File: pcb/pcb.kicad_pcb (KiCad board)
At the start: 2 copper layers, 299.5 x 123 mm, 72 parts

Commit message: A  RP2040_Minimal.kicad_sym A  RP2040_minimal.pretty/8-USON-Handsolder.kicad_mod A  RP2040_minimal.pretty/8-USON.kicad_mod A  RP2040_minimal.pretty/C_0402_1005Metric.kicad_mod A  RP2040_minimal.pretty/C_0603_1608Metric.kicad_mod A  RP2040_minimal.pretty/C_0603_1608Metric_Pad1.08x0.95mm_HandSolder.kicad_mod A  RP2040_minimal.pretty/C_1206_3216Metric.kicad_mod A  RP2040_minimal.pretty/Crystal_SMD_2520-4Pin_2.5x2.0mm-Handsolder.kicad_mod A  RP2040_minimal.pretty/Crystal_SMD_HC49-US.kicad_mod A  RP2040_minimal.pretty/D_0402_1005Metric.kicad_mod A  RP2040_minimal.pretty/D_SOD-523.kicad_mod A  RP2040_minimal.pretty/Diodes_U_DFN1212_3.kicad_mod A  RP2040_minimal.pretty/Diodes_U_DFN1212_3_Handsolder.kicad_mod A  RP2040_minimal.pretty/LED_0402_1005Metric.kicad_mod A  RP2040_minimal.pretty/LED_Driver_Mod_Conn.kicad_mod A  RP2040_minimal.pretty/LED_Driver_Mod_Conn_1.27.kicad_mod A  RP2040_minimal.pretty/Module_Conn_Regular.kicad_mod A  RP2040_minimal.pretty/Module_Conn_Regular2.kicad_mod A  RP2040_minimal.pretty/Module_Conn_Regular_Outline.kicad_mod A  RP2040_minimal.pretty/QFN-28-1EP_4x4mm_P0.4mm_EP2.3x2.3mm-Handsolder.kicad_mod A  RP2040_minimal.pretty/QFN-28-1EP_4x4mm_P0.4mm_EP2.3x2.3mm.kicad_mod A  RP2040_minimal.pretty/RP2040-QFN-56-Handsolder.kicad_mod A  RP2040_minimal.pretty/RP2040-QFN-56.kicad_mod A  RP2040_minimal.pretty/R_0402_1005Metric.kicad_mod A  RP2040_minimal.pretty/R_0603_1608Metric_Pad0.98x0.95mm_HandSolder.kicad_mod A  RP2040_minimal.pretty/SW_CK_KXT3.kicad_mod A  RP2040_minimal.pretty/SW_SPST_Panasonic_EVPAF.kicad_mod A  RP2040_minimal.pretty/SW_Side_EVPAV.kicad_mod A  RP2040_minimal.pretty/SW_XKB_TS_2030.kicad_mod A  RP2040_minimal.pretty/USB_Micro-B_Amphenol_10103594-0001LF_Horizontal_modified.kicad_mod A  RP2040_minimal.pretty/XSON-8-1EP_4x4mm.kicad_mod M  border.py M  notes/notes.md M  pcb/fp-lib-table M  pcb/pcb.kicad_pcb M  pcb/pcb.kicad_prl M  pcb/pcb.kicad_sch M  plate/plate.kicad_pcb M  plate/plate.kicad_sch R  tmr-footprints/Switch_Cutout2_MX.kic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
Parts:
- S64, S66: footprint tmr-lib:sw_lowpro_combo_MDT -> tmr-lib:sw_lowpro_combo_2u_MDT
- moved S63 2.32 mm to (95.6, 86.0), turned to -20 degrees
- moved S62 1.22 mm to (73.6, 76.0), turned to 0 degrees
- moved S68 1.22 mm to (199.5, 76.0), turned to 0 degrees
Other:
- board size 299.5 x 123 mm -> 299.2 x 113.4 mm

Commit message: M  border.py A  notes/keyfrequency M  pcb/pcb.kicad_pcb M  pcb/pcb.kicad_prl M  pcb/pcb.kicad_sch M  place.py A  tmr-footprints/LED-6028.kicad_mod D  tmr-footprints/LED_1206_THT.kicad_mod M  tmr-footprints/sw_lowpro_combo_2u_MDT.kicad_mod A  tmr-footprints/sw_lowpro_combo_2u_MDT_L.kicad_mod A  tmr-footprints/sw_lowpro_combo_2u_MDT_R.kicad_mod M  tmr-footprints/sw_lowpro_combo_MDT.kicad_mod M  tmr-footprints/sw_lowpro_combo_MDT_led.kicad_mod
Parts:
- S64: footprint tmr-lib:sw_lowpro_combo_2u_MDT -> tmr-lib:sw_lowpro_combo_2u_MDT_L
- S66: footprint tmr-lib:sw_lowpro_combo_2u_MDT -> tmr-lib:sw_lowpro_combo_2u_MDT_R
- moved S62 5.32 mm to (77.6, 79.5), turned to -20 degrees
- moved S59 4.25 mm to (11.4, 76.0)
- moved S68 3.91 mm to (197.8, 79.5), turned to 20 degrees
- moved S60 3.75 mm to (34.6, 76.0)
- moved S61 3.75 mm to (56.0, 76.0)
- moved S69 0.50 mm to (219.0, 76.0)
- moved S70 0.50 mm to (240.4, 76.0)
- moved S71 0.50 mm to (261.8, 76.0)
- moved S72 0.50 mm to (280.8, 76.0)
- turned S64 to -20 degrees
- turned S66 to 20 degrees
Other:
- board size 299.2 x 113.4 mm -> 299 x 113.3 mm

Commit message: M  border.py M  notes/components.md A  notes/mcu M  pcb/pcb.kicad_pcb M  place.py M  plate/plate.kicad_pcb M  plate/plate.kicad_sch
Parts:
- moved S1 2.38 mm to (16.6, 0.00)
- moved S60 0.40 mm to (35.0, 76.0)
- moved S61 0.40 mm to (56.4, 76.0)
- moved S71 0.10 mm to (261.9, 76.0)
- moved S72 0.10 mm to (280.9, 76.0)
- moved S59 0.10 mm to (11.3, 76.0)
- moved S69 0.10 mm to (219.1, 76.0)
- moved S70 0.10 mm to (240.5, 76.0)
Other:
- outline, holes or cut-outs redrawn

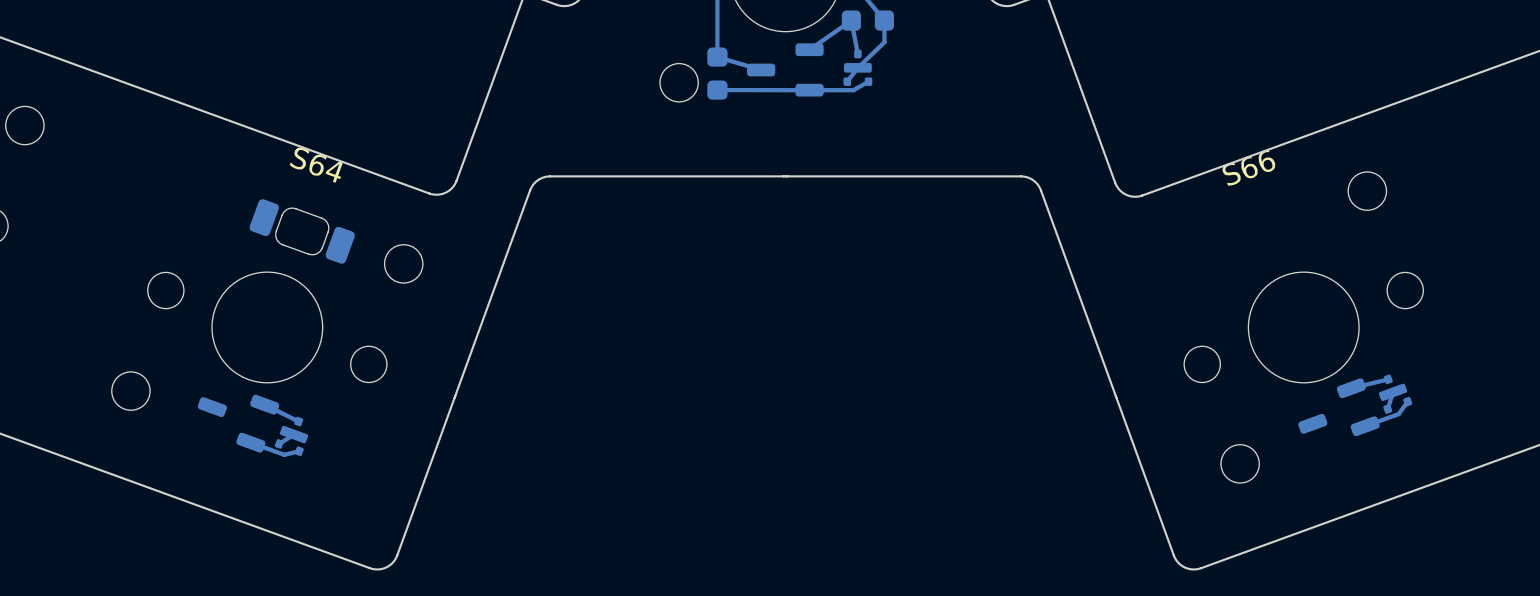
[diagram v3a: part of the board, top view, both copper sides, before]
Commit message: M  notes/components.md M  pcb/pcb.kicad_pcb M  pcb/pcb.kicad_sch M  place.py D  tmr-footprints/sw_lowpro_combo_2u_MDT.kicad_mod D  tmr-footprints/sw_lowpro_combo_2u_MDT_L.kicad_mod D  tmr-footprints/sw_lowpro_combo_2u_MDT_R.kicad_mod M  tmr-footprints/sw_lowpro_combo_MDT.kicad_mod A  tmr-footprints/sw_lowpro_stab_2u.kicad_mod M  tmr-symbols.kicad_sym
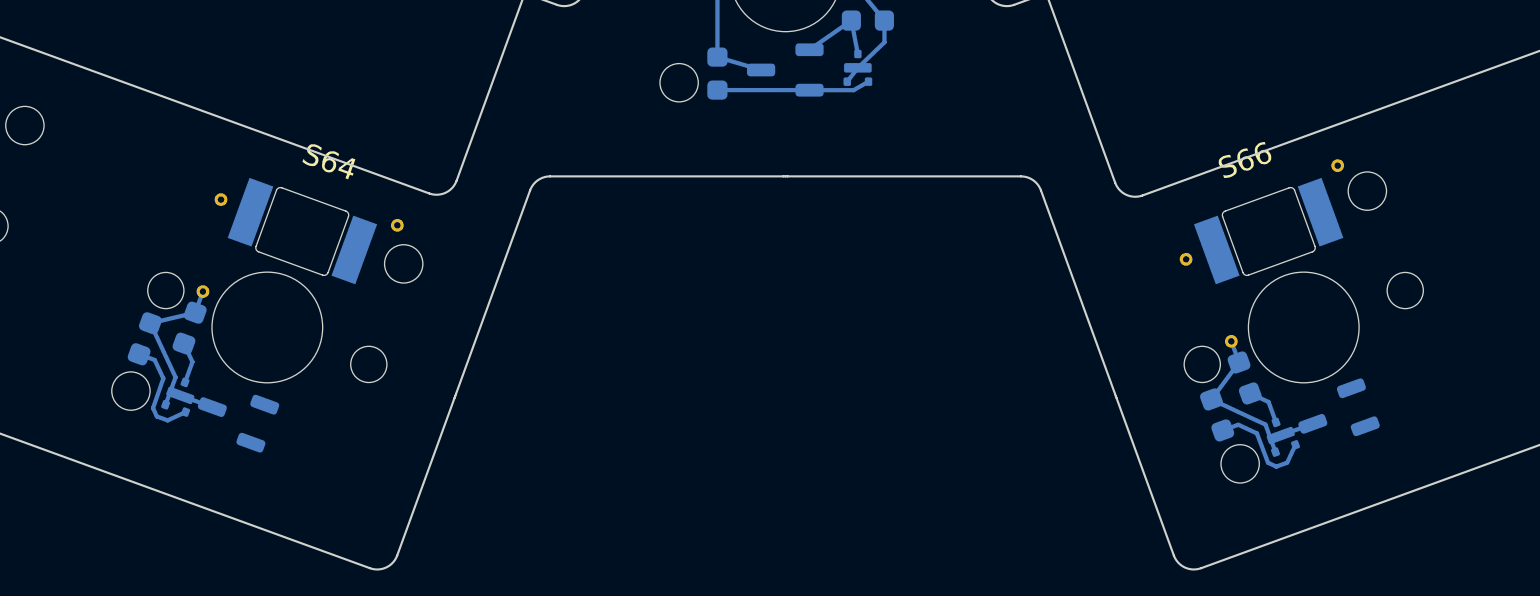
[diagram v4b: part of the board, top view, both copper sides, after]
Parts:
- added Stb1: TMR_switch_stab_2.0u, tmr-lib:sw_lowpro_stab_2u, F.Cu at (113.4, 92.5)
- added Stb2: TMR_switch_stab_2.0u, tmr-lib:sw_lowpro_stab_2u, F.Cu at (162.1, 92.5)
- S64: footprint tmr-lib:sw_lowpro_combo_2u_MDT_L -> tmr-lib:sw_lowpro_combo_MDT
- S66: footprint tmr-lib:sw_lowpro_combo_2u_MDT_R -> tmr-lib:sw_lowpro_combo_MDT

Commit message: M  border.py A  notes/cnc.md M  notes/components.md M  notes/nRF52840.md M  notes/notes.md A  notes/parts M  pcb/pcb.kicad_pcb M  plate/plate.kicad_pcb
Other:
- board size 299 x 113.3 mm -> 299.5 x 113.5 mm

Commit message: M  border.py M  notes/cnc.md M  notes/nRF52840.md M  notes/notes.md M  pcb/pcb.kicad_pcb M  pcb/pcb.kicad_sch M  pcb/sym-lib-table M  place.py M  plate/plate.kicad_pcb M  plate/plate.kicad_sch A  tmr-footprints/IS31FL3731-SSOP-28_5.3x10.2mm_P0.65mm.kicad_mod A  tmr-footprints/MCP3208-SOIC-16_3.9x9.9mm_P1.27mm.kicad_mod M  tmr-footprints/sw_lowpro_combo_MDT.kicad_mod D  tmr-footprints/sw_lowpro_combo_MDT_led.kicad_mod
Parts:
- added ADC1: MCP3208, tmr-lib:MCP3208-SOIC-16_3.9x9.9mm_P1.27mm, B.Cu at (56.1, 25.6)
- added ADC2: MCP3208, tmr-lib:MCP3208-SOIC-16_3.9x9.9mm_P1.27mm, F.Cu at (110.5, 129.5)
- added ADC3: MCP3208, tmr-lib:MCP3208-SOIC-16_3.9x9.9mm_P1.27mm, F.Cu at (119.0, 129.5)
- added ADC4: MCP3208, tmr-lib:MCP3208-SOIC-16_3.9x9.9mm_P1.27mm, F.Cu at (102.1, 141.2)
- added ADC5: MCP3208, tmr-lib:MCP3208-SOIC-16_3.9x9.9mm_P1.27mm, F.Cu at (110.5, 141.2)
- added ADC6: MCP3208, tmr-lib:MCP3208-SOIC-16_3.9x9.9mm_P1.27mm, F.Cu at (119.0, 141.2)
- added ADC7: MCP3208, tmr-lib:MCP3208-SOIC-16_3.9x9.9mm_P1.27mm, F.Cu at (102.1, 152.8)
- added ADC8: MCP3208, tmr-lib:MCP3208-SOIC-16_3.9x9.9mm_P1.27mm, F.Cu at (110.5, 152.8)
- added ADC9: MCP3208, tmr-lib:MCP3208-SOIC-16_3.9x9.9mm_P1.27mm, F.Cu at (119.0, 152.8)
- added D1: LED, tmr-lib:LED-6028, F.Cu at (55.3, 126.0)
- added D10: LED, tmr-lib:LED-6028, F.Cu at (55.3, 168.8)
- added D11: LED, tmr-lib:LED-6028, F.Cu at (55.3, 173.5)
- added D12: LED, tmr-lib:LED-6028, F.Cu at (55.3, 178.3)
- added D13: LED, tmr-lib:LED-6028, F.Cu at (63.1, 126.0)
- added D14: LED, tmr-lib:LED-6028, F.Cu at (63.1, 130.8)
- added D15: LED, tmr-lib:LED-6028, F.Cu at (63.1, 135.5)
- added D16: LED, tmr-lib:LED-6028, F.Cu at (63.1, 140.3)
- added D17: LED, tmr-lib:LED-6028, F.Cu at (63.1, 145.0)
- added D18: LED, tmr-lib:LED-6028, F.Cu at (63.1, 149.8)
- added D19: LED, tmr-lib:LED-6028, F.Cu at (63.1, 154.5)
- added D2: LED, tmr-lib:LED-6028, F.Cu at (55.3, 130.8)
- added D20: LED, tmr-lib:LED-6028, F.Cu at (63.1, 159.3)
- added D21: LED, tmr-lib:LED-6028, F.Cu at (63.1, 164.0)
- added D22: LED, tmr-lib:LED-6028, F.Cu at (63.1, 168.8)
- added D23: LED, tmr-lib:LED-6028, F.Cu at (63.1, 173.5)
- added D24: LED, tmr-lib:LED-6028, F.Cu at (63.1, 178.3)
- added D25: LED, tmr-lib:LED-6028, F.Cu at (70.8, 126.0)
- added D26: LED, tmr-lib:LED-6028, F.Cu at (70.8, 130.8)
- added D27: LED, tmr-lib:LED-6028, F.Cu at (70.8, 135.5)
- added D28: LED, tmr-lib:LED-6028, F.Cu at (70.8, 140.3)
- added D29: LED, tmr-lib:LED-6028, F.Cu at (70.8, 145.0)
- added D3: LED, tmr-lib:LED-6028, F.Cu at (55.3, 135.5)
- added D30: LED, tmr-lib:LED-6028, F.Cu at (70.8, 149.8)
- added D31: LED, tmr-lib:LED-6028, F.Cu at (70.8, 154.5)
- added D32: LED, tmr-lib:LED-6028, F.Cu at (70.8, 159.3)
- added D33: LED, tmr-lib:LED-6028, F.Cu at (70.8, 164.0)
- added D34: LED, tmr-lib:LED-6028, F.Cu at (70.8, 168.8)
- added D35: LED, tmr-lib:LED-6028, F.Cu at (70.8, 173.5)
- added D36: LED, tmr-lib:LED-6028, F.Cu at (70.8, 178.3)
- added D37: LED, tmr-lib:LED-6028, F.Cu at (78.6, 126.0)
- added D38: LED, tmr-lib:LED-6028, F.Cu at (78.6, 130.8)
- added D39: LED, tmr-lib:LED-6028, F.Cu at (78.6, 135.5)
- added D4: LED, tmr-lib:LED-6028, F.Cu at (55.3, 140.3)
- added D40: LED, tmr-lib:LED-6028, F.Cu at (78.6, 140.3)
- added D41: LED, tmr-lib:LED-6028, F.Cu at (78.6, 145.0)
- added D42: LED, tmr-lib:LED-6028, F.Cu at (78.6, 149.8)
- added D43: LED, tmr-lib:LED-6028, F.Cu at (78.6, 154.5)
- added D44: LED, tmr-lib:LED-6028, F.Cu at (78.6, 159.3)
- added D45: LED, tmr-lib:LED-6028, F.Cu at (78.6, 164.0)
- added D46: LED, tmr-lib:LED-6028, F.Cu at (78.6, 168.8)
- added D47: LED, tmr-lib:LED-6028, F.Cu at (78.6, 173.5)
- added D48: LED, tmr-lib:LED-6028, F.Cu at (78.6, 178.3)
- added D49: LED, tmr-lib:LED-6028, F.Cu at (86.4, 126.0)
- added D5: LED, tmr-lib:LED-6028, F.Cu at (55.3, 145.0)
- added D50: LED, tmr-lib:LED-6028, F.Cu at (86.4, 130.8)
- added D51: LED, tmr-lib:LED-6028, F.Cu at (86.4, 135.5)
- added D52: LED, tmr-lib:LED-6028, F.Cu at (86.4, 140.3)
- added D53: LED, tmr-lib:LED-6028, F.Cu at (86.4, 145.0)
- added D54: LED, tmr-lib:LED-6028, F.Cu at (86.4, 149.8)
- added D55: LED, tmr-lib:LED-6028, F.Cu at (86.4, 154.5)
- added D56: LED, tmr-lib:LED-6028, F.Cu at (86.4, 159.3)
- added D57: LED, tmr-lib:LED-6028, F.Cu at (86.4, 164.0)
- added D58: LED, tmr-lib:LED-6028, F.Cu at (86.4, 168.8)
- added D59: LED, tmr-lib:LED-6028, F.Cu at (86.4, 173.5)
- added D6: LED, tmr-lib:LED-6028, F.Cu at (55.3, 149.8)
- added D60: LED, tmr-lib:LED-6028, F.Cu at (86.4, 178.3)
- added D61: LED, tmr-lib:LED-6028, F.Cu at (94.1, 126.0)
- added D62: LED, tmr-lib:LED-6028, F.Cu at (94.1, 130.8)
- added D63: LED, tmr-lib:LED-6028, F.Cu at (94.1, 135.5)
- added D64: LED, tmr-lib:LED-6028, F.Cu at (94.1, 140.3)
- added D65: LED, tmr-lib:LED-6028, F.Cu at (94.1, 145.0)
- added D66: LED, tmr-lib:LED-6028, F.Cu at (94.1, 149.8)
- added D67: LED, tmr-lib:LED-6028, F.Cu at (94.1, 154.5)
- added D68: LED, tmr-lib:LED-6028, F.Cu at (94.1, 159.3)
- added D69: LED, tmr-lib:LED-6028, F.Cu at (94.1, 164.0)
- added D7: LED, tmr-lib:LED-6028, F.Cu at (55.3, 154.5)
- added D70: LED, tmr-lib:LED-6028, F.Cu at (94.1, 168.8)
- added D71: LED, tmr-lib:LED-6028, F.Cu at (94.1, 173.5)
- added D72: LED, tmr-lib:LED-6028, F.Cu at (94.1, 178.3)
- added D8: LED, tmr-lib:LED-6028, F.Cu at (55.3, 159.3)
- added D9: LED, tmr-lib:LED-6028, F.Cu at (55.3, 164.0)
- added LedDr1: IS31FL3731-QF, tmr-lib:IS31FL3731-SSOP-28_5.3x10.2mm_P0.65mm, F.Cu at (103.1, 164.4)
- added USBCon1: USB_TYPE_C_Receptacle_16P, Connector_USB:USB_C_Receptacle_XKB_U262-16XN-4BVC11, B.Cu at (28.5, -6.08)
- moved S1 2.38 mm to (19.0, 0.00)
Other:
- outline, holes or cut-outs redrawn

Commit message: M  border.py M  notes/notes.md M  pcb/pcb.kicad_pcb M  pcb/pcb.kicad_prl M  pcb/pcb.kicad_pro M  pcb/pcb.kicad_sch M  pcb/sym-lib-table M  place.py M  tmr-footprints/C_0603_1608Metric.kicad_mod D  tmr-footprints/C_0805_2012Metric.kicad_mod A  tmr-footprints/C_1206_3216Metric.kicad_mod A  tmr-footprints/IS31FL3731-RECESSED-SSOP-28_5.3x10.2mm_P0.65mm.kicad_mod M  tmr-footprints/JLC_Order_Num.kicad_mod M  tmr-footprints/LED-6028.kicad_mod A  tmr-footprints/MCP3208-RECESSED-SOIC-16_3.9x9.9mm_P1.27mm.kicad_mod M  tmr-footprints/MCP3208-SOIC-16_3.9x9.9mm_P1.27mm.kicad_mod A  tmr-footprints/MountingHole_5.3mm_M5_ISO14580_Pad_TopBottom.kicad_mod A  tmr-footprints/R_0603_1608Metric.kicad_mod A  tmr-footprints/SMTSO_M1.6.kicad_mod A  tmr-footprints/SW_B3U-3000P.kicad_mod A  tmr-footprints/sw_lowpro_gateron_MDT.kicad_mod M  tmr-symbols.kicad_sym
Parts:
- removed the ADC5 at (110.5, 141.2)
- added ADC3: MCP3208, tmr-lib:MCP3208-SOIC-16_3.9x9.9mm_P1.27mm, B.Cu at (48.1, 54.3)
- added C1: C_Small_US, tmr-lib:C_0603_1608Metric, F.Cu at (215.0, 94.0)
- added C10: 100nF, tmr-lib:C_0603_1608Metric, F.Cu at (215.0, 116.6)
- added C11: 100nF, tmr-lib:C_0603_1608Metric, F.Cu at (219.0, 94.0)
- added C12: 100nF, tmr-lib:C_0603_1608Metric, F.Cu at (219.0, 96.5)
- added C13: 100nF, tmr-lib:C_0603_1608Metric, F.Cu at (219.0, 99.0)
- added C14: 100nF, tmr-lib:C_0603_1608Metric, F.Cu at (219.0, 101.5)
- added C15: 100nF, tmr-lib:C_0603_1608Metric, F.Cu at (219.0, 104.0)
- added C16: 100nF, tmr-lib:C_0603_1608Metric, F.Cu at (219.0, 106.5)
- added C17: 100nF, tmr-lib:C_0603_1608Metric, F.Cu at (219.0, 109.1)
- added C18: 100nF, tmr-lib:C_0603_1608Metric, F.Cu at (219.0, 111.6)
- added C19: 2.2uF, tmr-lib:C_0603_1608Metric, F.Cu at (219.0, 114.1)
- added C2: C_Small_US, tmr-lib:C_0603_1608Metric, F.Cu at (215.0, 96.5)
- added C20: 1uF, tmr-lib:C_0603_1608Metric, F.Cu at (219.0, 116.6)
- added C21: 1uF, tmr-lib:C_0603_1608Metric, F.Cu at (223.1, 94.0)
- added C22: 100nF, tmr-lib:C_0603_1608Metric, F.Cu at (223.1, 96.5)
- added C23: 2.2uF, tmr-lib:C_0603_1608Metric, F.Cu at (223.1, 99.0)
- added C24: 10uF, tmr-lib:C_0603_1608Metric, F.Cu at (223.1, 101.5)
- added C25: 2.2uF, tmr-lib:C_0603_1608Metric, F.Cu at (223.1, 104.0)
- added C26: 1uF, tmr-lib:C_0603_1608Metric, F.Cu at (223.1, 106.5)
- added C27: 10uF, tmr-lib:C_1206_3216Metric, F.Cu at (206.5, 94.7)
- added C28: 10uF, tmr-lib:C_0603_1608Metric, F.Cu at (223.1, 109.1)
- added C29: 100nF, tmr-lib:C_0603_1608Metric, F.Cu at (223.1, 111.6)
- added C3: C_Small_US, tmr-lib:C_0603_1608Metric, F.Cu at (215.0, 99.0)
- added C30: 100nF, tmr-lib:C_0603_1608Metric, F.Cu at (223.1, 114.1)
- added C31: 15pF, tmr-lib:C_0603_1608Metric, F.Cu at (28.3, 62.9)
- added C32: 15pF, tmr-lib:C_0603_1608Metric, F.Cu at (28.6, 56.6)
- added C4: C_Small_US, tmr-lib:C_0603_1608Metric, F.Cu at (215.0, 101.5)
- added C5: C_Small_US, tmr-lib:C_0603_1608Metric, F.Cu at (215.0, 104.0)
- added C6: C_Small_US, tmr-lib:C_0603_1608Metric, F.Cu at (215.0, 106.5)
- added C7: C_Small_US, tmr-lib:C_0603_1608Metric, F.Cu at (215.0, 109.1)
- added C8: C_Small_US, tmr-lib:C_0603_1608Metric, F.Cu at (215.0, 111.6)
- added C9: C_Small_US, tmr-lib:C_0603_1608Metric, F.Cu at (215.0, 114.1)
- added H1: MountingHole, tmr-lib:MountingHole_5.3mm_M5_ISO14580_Pad_TopBottom, F.Cu at (85.5, 8.93)
- added H2: MountingHole, tmr-lib:MountingHole_5.3mm_M5_ISO14580_Pad_TopBottom, F.Cu at (237.5, 8.93)
- added H3: MountingHole, tmr-lib:MountingHole_5.3mm_M5_ISO14580_Pad_TopBottom, F.Cu at (291.6, 25.6)
- added H4: MountingHole, tmr-lib:MountingHole_5.3mm_M5_ISO14580_Pad_TopBottom, F.Cu at (12.3, 25.6)
- added H5: MountingHole, tmr-lib:MountingHole_5.3mm_M5_ISO14580_Pad_TopBottom, F.Cu at (99.8, 46.9)
- added H6: MountingHole, tmr-lib:MountingHole_5.3mm_M5_ISO14580_Pad_TopBottom, F.Cu at (175.8, 46.9)
- added H7: MountingHole, tmr-lib:MountingHole_5.3mm_M5_ISO14580_Pad_TopBottom, F.Cu at (1.90, 82.6)
- added H8: MountingHole, tmr-lib:MountingHole_5.3mm_M5_ISO14580_Pad_TopBottom, F.Cu at (251.2, 82.6)
- added Hs1: ~, tmr-lib:SMTSO_M1.6, F.Cu at (28.5, 8.93)
- added Hs10: ~, tmr-lib:SMTSO_M1.6, F.Cu at (275.5, 65.9)
- added Hs11, Hs12, Hs13, Hs14, Hs15, Hs16, Hs17, Hs18: ~, tmr-lib:SMTSO_M1.6, F.Cu at (0.00, 0.00)
- added Hs2: ~, tmr-lib:SMTSO_M1.6, F.Cu at (142.5, 8.93)
- added Hs3: ~, tmr-lib:SMTSO_M1.6, F.Cu at (275.5, 8.93)
- added Hs4: ~, tmr-lib:SMTSO_M1.6, F.Cu at (1.90, 76.0)
- added Hs5: ~, tmr-lib:SMTSO_M1.6, F.Cu at (61.8, 46.9)
- added Hs6: ~, tmr-lib:SMTSO_M1.6, F.Cu at (137.8, 46.9)
- added Hs7: ~, tmr-lib:SMTSO_M1.6, F.Cu at (86.4, 83.6)
- added Hs8: ~, tmr-lib:SMTSO_M1.6, F.Cu at (189.1, 83.6)
- added Hs9: ~, tmr-lib:SMTSO_M1.6, F.Cu at (209.0, 27.9)
- added JLC1: JLC_Order_Num, tmr-lib:JLC_Order_Num, F.Cu at (233.8, 161.6)
- added R1: 10k, tmr-lib:R_0603_1608Metric, B.Cu at (20.0, 91.5)
- added R10: 4.7k, tmr-lib:R_0603_1608Metric, B.Cu at (250.9, 68.6)
- added R11: 100k, tmr-lib:R_0603_1608Metric, B.Cu at (250.9, 71.1)
- added R12: 20k, tmr-lib:R_0603_1608Metric, B.Cu at (250.9, 73.6)
- added R13: 20k, tmr-lib:R_0603_1608Metric, B.Cu at (250.9, 76.1)
- added R14: 1k, tmr-lib:R_0603_1608Metric, B.Cu at (25.6, 61.6)
- added R2: 10k, tmr-lib:R_0603_1608Metric, B.Cu at (20.0, 94.0)
- added R3: 1k, tmr-lib:R_0603_1608Metric, B.Cu at (20.0, 96.5)
- added R4: 27R, tmr-lib:R_0603_1608Metric, B.Cu at (20.0, 99.1)
- added R5: 27R, tmr-lib:R_0603_1608Metric, B.Cu at (20.0, 101.6)
- added R6: 5.1k, tmr-lib:R_0603_1608Metric, B.Cu at (20.0, 104.1)
- added R7: 5.1k, tmr-lib:R_0603_1608Metric, B.Cu at (20.0, 106.6)
- added R8: 4.7k, tmr-lib:R_0603_1608Metric, B.Cu at (20.0, 109.1)
- added R9: 4.7k, tmr-lib:R_0603_1608Metric, B.Cu at (20.0, 111.6)
- added SW1: SW_DIP_x01_XKB_TS_2030, Button_Switch_SMD:SW_SPST_B3U-3000P, F.Cu at (1.95, 36.8)
- added SW2: SW_DIP_x01_XKB_TS_2030, Button_Switch_SMD:SW_SPST_B3U-3000P, F.Cu at (1.90, 41.9)
- added U1: RP2040, rp2040:RP2040-QFN-56, B.Cu at (21.4, 56.9)
- added U2: Memory_Flash_W25Q64_XSON, rp2040:8-USON, B.Cu at (20.5, 48.2)
- added U3: NCP114ASN330T1G, Package_SO:TSOP-5_1.65x3.05mm_P0.95mm, F.Cu at (1.99, 67.2)
- added X1: 12.000MHz, rp2040:Crystal_SMD_2520-4Pin_2.5x2.0mm-Handsolder, B.Cu at (28.7, 60.1)
- ADC2, ADC4, ADC6, ADC7, ADC8, ADC9: moved to B.Cu
- ADC5: renamed from ADC3; moved to B.Cu
- LedDr1: footprint tmr-lib:IS31FL3731-SSOP-28_5.3x10.2mm_P0.65mm -> rp2040:QFN-28-1EP_4x4mm_P0.4mm_EP2.3x2.3mm; moved to B.Cu
- S1, S10, S11, S12, S13, S14, S15, S16, S17, S18, S19, S2, S20, S21, S22, S23, S24, S25, S26, S27, S28, S29, S3, S30, S31, S32, S33, S34, S35, S36, S37, S38, S39, S4, S40, S41, S42, S43, S44, S45, S46, S47, S48, S49, S5, S50, S51, S52, S53, S54, S55, S56, S57, S58, S59, S6, S60, S61, S62, S63, S64, S65, S66, S67, S68, S69, S7, S70, S71, S72, S8, S9: footprint tmr-lib:sw_lowpro_combo_MDT -> tmr-lib:sw_lowpro_gateron_MDT
- moved D15 262.5 mm to (285.0, -4.75)
- moved D12 251.6 mm to (228.0, -4.75)
- moved D29 246.9 mm to (280.2, 14.2)
- moved D14 244.0 mm to (266.0, -4.75)
- moved D44 241.8 mm to (285.0, 33.2)
- moved D11 235.4 mm to (209.0, -4.75)
- moved D58 230.3 mm to (285.0, 52.2)
- moved D13 225.7 mm to (247.0, -4.75)
- moved D28 224.4 mm to (256.5, 14.2)
- moved D43 223.2 mm to (266.0, 33.2)
- moved D10 219.6 mm to (190.0, -4.75)
- moved D72 215.2 mm to (280.9, 71.2)
- moved D27 206.1 mm to (237.5, 14.2)
- moved D57 205.5 mm to (258.9, 52.2)
- moved D9 204.6 mm to (171.0, -4.75)
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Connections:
- ADC1 pad 14: unconnected-(ADC1-AGND-Pad14) -> GND
- ADC1 pad 15: unconnected-(ADC1-Vref-Pad15) -> +3V3
- ADC1 pad 16: unconnected-(ADC1-Vdd-Pad16) -> +3V3
- ADC1 pad 9: unconnected-(ADC1-DGND-Pad9) -> GND
- ADC2 pad 14: unconnected-(ADC2-AGND-Pad14) -> GND
- ADC2 pad 15: unconnected-(ADC2-Vref-Pad15) -> +3V3
- ADC2 pad 16: unconnected-(ADC2-Vdd-Pad16) -> +3V3
- ADC2 pad 9: unconnected-(ADC2-DGND-Pad9) -> GND
- ADC4 pad 14: unconnected-(ADC4-AGND-Pad14) -> GND
- ADC4 pad 15: unconnected-(ADC4-Vref-Pad15) -> +3V3
- ADC4 pad 16: unconnected-(ADC4-Vdd-Pad16) -> +3V3
- ADC4 pad 9: unconnected-(ADC4-DGND-Pad9) -> GND
- ADC5 pad 14: unconnected-(ADC3-AGND-Pad14) -> GND
- ADC5 pad 15: unconnected-(ADC3-Vref-Pad15) -> +3V3
- ADC5 pad 16: unconnected-(ADC3-Vdd-Pad16) -> +3V3
- ADC5 pad 9: unconnected-(ADC3-DGND-Pad9) -> GND
- ADC6 pad 14: unconnected-(ADC6-AGND-Pad14) -> GND
- ADC6 pad 15: unconnected-(ADC6-Vref-Pad15) -> +3V3
- ADC6 pad 16: unconnected-(ADC6-Vdd-Pad16) -> +3V3
- ADC6 pad 9: unconnected-(ADC6-DGND-Pad9) -> GND
- ADC7 pad 14: unconnected-(ADC7-AGND-Pad14) -> GND
- ADC7 pad 15: unconnected-(ADC7-Vref-Pad15) -> +3V3
- ADC7 pad 16: unconnected-(ADC7-Vdd-Pad16) -> +3V3
- ADC7 pad 9: unconnected-(ADC7-DGND-Pad9) -> GND
- ADC8 pad 14: unconnected-(ADC8-AGND-Pad14) -> GND
- ADC8 pad 15: unconnected-(ADC8-Vref-Pad15) -> +3V3
- ADC8 pad 16: unconnected-(ADC8-Vdd-Pad16) -> +3V3
- ADC8 pad 9: unconnected-(ADC8-DGND-Pad9) -> GND
- ADC9 pad 14: unconnected-(ADC9-AGND-Pad14) -> GND
- ADC9 pad 15: unconnected-(ADC9-Vref-Pad15) -> +3V3
- ADC9 pad 16: unconnected-(ADC9-Vdd-Pad16) -> +3V3
- ADC9 pad 9: unconnected-(ADC9-DGND-Pad9) -> GND
- S1 pad 1: unconnected-(S1-V_{CC}-Pad1) -> +3V3
- S1 pad 3: unconnected-(S1-GND-Pad3) -> GND
- S10 pad 1: unconnected-(S10-V_{CC}-Pad1) -> +3V3
- S10 pad 3: unconnected-(S10-GND-Pad3) -> GND
- S11 pad 1: unconnected-(S11-V_{CC}-Pad1) -> +3V3
- S11 pad 3: unconnected-(S11-GND-Pad3) -> GND
- S12 pad 1: unconnected-(S12-V_{CC}-Pad1) -> +3V3
- S12 pad 3: unconnected-(S12-GND-Pad3) -> GND
- S13 pad 1: unconnected-(S13-V_{CC}-Pad1) -> +3V3
- S13 pad 3: unconnected-(S13-GND-Pad3) -> GND
- S14 pad 1: unconnected-(S14-V_{CC}-Pad1) -> +3V3
- S14 pad 3: unconnected-(S14-GND-Pad3) -> GND
- S15 pad 1: unconnected-(S15-V_{CC}-Pad1) -> +3V3
- S15 pad 3: unconnected-(S15-GND-Pad3) -> GND
- S16 pad 1: unconnected-(S16-V_{CC}-Pad1) -> +3V3
- S16 pad 3: unconnected-(S16-GND-Pad3) -> GND
- S17 pad 1: unconnected-(S17-V_{CC}-Pad1) -> +3V3
- S17 pad 3: unconnected-(S17-GND-Pad3) -> GND
- S18 pad 1: unconnected-(S18-V_{CC}-Pad1) -> +3V3
- S18 pad 3: unconnected-(S18-GND-Pad3) -> GND
- S19 pad 1: unconnected-(S19-V_{CC}-Pad1) -> +3V3
- S19 pad 3: unconnected-(S19-GND-Pad3) -> GND
- S2 pad 1: unconnected-(S2-V_{CC}-Pad1) -> +3V3
- S2 pad 3: unconnected-(S2-GND-Pad3) -> GND
- S20 pad 1: unconnected-(S20-V_{CC}-Pad1) -> +3V3
- S20 pad 3: unconnected-(S20-GND-Pad3) -> GND
- S21 pad 1: unconnected-(S21-V_{CC}-Pad1) -> +3V3
- S21 pad 3: unconnected-(S21-GND-Pad3) -> GND
- S22 pad 1: unconnected-(S22-V_{CC}-Pad1) -> +3V3
- S22 pad 3: unconnected-(S22-GND-Pad3) -> GND
- S23 pad 1: unconnected-(S23-V_{CC}-Pad1) -> +3V3
- S23 pad 3: unconnected-(S23-GND-Pad3) -> GND
- S24 pad 1: unconnected-(S24-V_{CC}-Pad1) -> +3V3
- S24 pad 3: unconnected-(S24-GND-Pad3) -> GND
- S25 pad 1: unconnected-(S25-V_{CC}-Pad1) -> +3V3
- S25 pad 3: unconnected-(S25-GND-Pad3) -> GND
- S26 pad 1: unconnected-(S26-V_{CC}-Pad1) -> +3V3
- S26 pad 3: unconnected-(S26-GND-Pad3) -> GND
- S27 pad 1: unconnected-(S27-V_{CC}-Pad1) -> +3V3
- S27 pad 3: unconnected-(S27-GND-Pad3) -> GND
- S28 pad 1: unconnected-(S28-V_{CC}-Pad1) -> +3V3
- S28 pad 3: unconnected-(S28-GND-Pad3) -> GND
- S29 pad 1: unconnected-(S29-V_{CC}-Pad1) -> +3V3
- S29 pad 3: unconnected-(S29-GND-Pad3) -> GND
- S3 pad 1: unconnected-(S3-V_{CC}-Pad1) -> +3V3
- S3 pad 3: unconnected-(S3-GND-Pad3) -> GND
- S30 pad 1: unconnected-(S30-V_{CC}-Pad1) -> +3V3
- S30 pad 3: unconnected-(S30-GND-Pad3) -> GND
- S31 pad 1: unconnected-(S31-V_{CC}-Pad1) -> +3V3
- S31 pad 3: unconnected-(S31-GND-Pad3) -> GND
- S32 pad 1: unconnected-(S32-V_{CC}-Pad1) -> +3V3
- S32 pad 3: unconnected-(S32-GND-Pad3) -> GND
- S33 pad 1: unconnected-(S33-V_{CC}-Pad1) -> +3V3
- S33 pad 3: unconnected-(S33-GND-Pad3) -> GND
- S34 pad 1: unconnected-(S34-V_{CC}-Pad1) -> +3V3
- S34 pad 3: unconnected-(S34-GND-Pad3) -> GND
- S35 pad 1: unconnected-(S35-V_{CC}-Pad1) -> +3V3
- S35 pad 3: unconnected-(S35-GND-Pad3) -> GND
- S36 pad 1: unconnected-(S36-V_{CC}-Pad1) -> +3V3
- S36 pad 3: unconnected-(S36-GND-Pad3) -> GND
- S37 pad 1: unconnected-(S37-V_{CC}-Pad1) -> +3V3
- S37 pad 3: unconnected-(S37-GND-Pad3) -> GND
- S38 pad 1: unconnected-(S38-V_{CC}-Pad1) -> +3V3
- S38 pad 3: unconnected-(S38-GND-Pad3) -> GND
- S39 pad 1: unconnected-(S39-V_{CC}-Pad1) -> +3V3
- S39 pad 3: unconnected-(S39-GND-Pad3) -> GND
- S4 pad 1: unconnected-(S4-V_{CC}-Pad1) -> +3V3
- S4 pad 3: unconnected-(S4-GND-Pad3) -> GND
- S40 pad 1: unconnected-(S40-V_{CC}-Pad1) -> +3V3
- S40 pad 3: unconnected-(S40-GND-Pad3) -> GND
- S41 pad 1: unconnected-(S41-V_{CC}-Pad1) -> +3V3
- S41 pad 3: unconnected-(S41-GND-Pad3) -> GND
- S42 pad 1: unconnected-(S42-V_{CC}-Pad1) -> +3V3
- S42 pad 3: unconnected-(S42-GND-Pad3) -> GND
- S43 pad 1: unconnected-(S43-V_{CC}-Pad1) -> +3V3
- S43 pad 3: unconnected-(S43-GND-Pad3) -> GND
- S44 pad 1: unconnected-(S44-V_{CC}-Pad1) -> +3V3
- S44 pad 3: unconnected-(S44-GND-Pad3) -> GND
- S45 pad 1: unconnected-(S45-V_{CC}-Pad1) -> +3V3
- S45 pad 3: unconnected-(S45-GND-Pad3) -> GND
- S46 pad 1: unconnected-(S46-V_{CC}-Pad1) -> +3V3
- S46 pad 3: unconnected-(S46-GND-Pad3) -> GND
- S47 pad 1: unconnected-(S47-V_{CC}-Pad1) -> +3V3
- S47 pad 3: unconnected-(S47-GND-Pad3) -> GND
- S48 pad 1: unconnected-(S48-V_{CC}-Pad1) -> +3V3
- S48 pad 3: unconnected-(S48-GND-Pad3) -> GND
- S49 pad 1: unconnected-(S49-V_{CC}-Pad1) -> +3V3
- S49 pad 3: unconnected-(S49-GND-Pad3) -> GND
- S5 pad 1: unconnected-(S5-V_{CC}-Pad1) -> +3V3
- S5 pad 3: unconnected-(S5-GND-Pad3) -> GND
- S50 pad 1: unconnected-(S50-V_{CC}-Pad1) -> +3V3
- S50 pad 3: unconnected-(S50-GND-Pad3) -> GND
- S51 pad 1: unconnected-(S51-V_{CC}-Pad1) -> +3V3
- S51 pad 3: unconnected-(S51-GND-Pad3) -> GND
- S52 pad 1: unconnected-(S52-V_{CC}-Pad1) -> +3V3
- S52 pad 3: unconnected-(S52-GND-Pad3) -> GND
- S53 pad 1: unconnected-(S53-V_{CC}-Pad1) -> +3V3
- S53 pad 3: unconnected-(S53-GND-Pad3) -> GND
- S54 pad 1: unconnected-(S54-V_{CC}-Pad1) -> +3V3
- S54 pad 3: unconnected-(S54-GND-Pad3) -> GND
- S55 pad 1: unconnected-(S55-V_{CC}-Pad1) -> +3V3
- S55 pad 3: unconnected-(S55-GND-Pad3) -> GND
- S56 pad 1: unconnected-(S56-V_{CC}-Pad1) -> +3V3
- S56 pad 3: unconnected-(S56-GND-Pad3) -> GND
- S57 pad 1: unconnected-(S57-V_{CC}-Pad1) -> +3V3
- S57 pad 3: unconnected-(S57-GND-Pad3) -> GND
- S58 pad 1: unconnected-(S58-V_{CC}-Pad1) -> +3V3
- S58 pad 3: unconnected-(S58-GND-Pad3) -> GND
- S59 pad 1: unconnected-(S59-V_{CC}-Pad1) -> +3V3
- S59 pad 3: unconnected-(S59-GND-Pad3) -> GND
- S6 pad 1: unconnected-(S6-V_{CC}-Pad1) -> +3V3
- S6 pad 3: unconnected-(S6-GND-Pad3) -> GND
- S60 pad 1: unconnected-(S60-V_{CC}-Pad1) -> +3V3
- S60 pad 3: unconnected-(S60-GND-Pad3) -> GND
- S61 pad 1: unconnected-(S61-V_{CC}-Pad1) -> +3V3
- S61 pad 3: unconnected-(S61-GND-Pad3) -> GND
- S62 pad 1: unconnected-(S62-V_{CC}-Pad1) -> +3V3
- S62 pad 3: unconnected-(S62-GND-Pad3) -> GND
- S63 pad 1: unconnected-(S63-V_{CC}-Pad1) -> +3V3
- S63 pad 3: unconnected-(S63-GND-Pad3) -> GND
- S64 pad 1: unconnected-(S64-V_{CC}-Pad1) -> +3V3
- S64 pad 3: unconnected-(S64-GND-Pad3) -> GND
- S65 pad 1: unconnected-(S65-V_{CC}-Pad1) -> +3V3
- S65 pad 3: unconnected-(S65-GND-Pad3) -> GND
- S66 pad 1: unconnected-(S66-V_{CC}-Pad1) -> +3V3
- S66 pad 3: unconnected-(S66-GND-Pad3) -> GND
- S67 pad 1: unconnected-(S67-V_{CC}-Pad1) -> +3V3
- S67 pad 3: unconnected-(S67-GND-Pad3) -> GND
- S68 pad 1: unconnected-(S68-V_{CC}-Pad1) -> +3V3
- S68 pad 3: unconnected-(S68-GND-Pad3) -> GND
- S69 pad 1: unconnected-(S69-V_{CC}-Pad1) -> +3V3
- S69 pad 3: unconnected-(S69-GND-Pad3) -> GND
- S7 pad 1: unconnected-(S7-V_{CC}-Pad1) -> +3V3
- S7 pad 3: unconnected-(S7-GND-Pad3) -> GND
- S70 pad 1: unconnected-(S70-V_{CC}-Pad1) -> +3V3
- S70 pad 3: unconnected-(S70-GND-Pad3) -> GND
- S71 pad 1: unconnected-(S71-V_{CC}-Pad1) -> +3V3
- S71 pad 3: unconnected-(S71-GND-Pad3) -> GND
- S72 pad 1: unconnected-(S72-V_{CC}-Pad1) -> +3V3
- S72 pad 3: unconnected-(S72-GND-Pad3) -> GND
- S8 pad 1: unconnected-(S8-V_{CC}-Pad1) -> +3V3
- S8 pad 3: unconnected-(S8-GND-Pad3) -> GND
- S9 pad 1: unconnected-(S9-V_{CC}-Pad1) -> +3V3
- S9 pad 3: unconnected-(S9-GND-Pad3) -> GND
